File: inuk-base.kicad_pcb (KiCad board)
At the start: 2 copper layers, 159.8 x 99.8 mm, 11 parts, among them J1 Conn_02x05_Odd_Even, J2 Conn_01x06, J3 Conn_01x02_Male, J4 Conn_01x02_Male, U1 E73-2G4M04S-52832

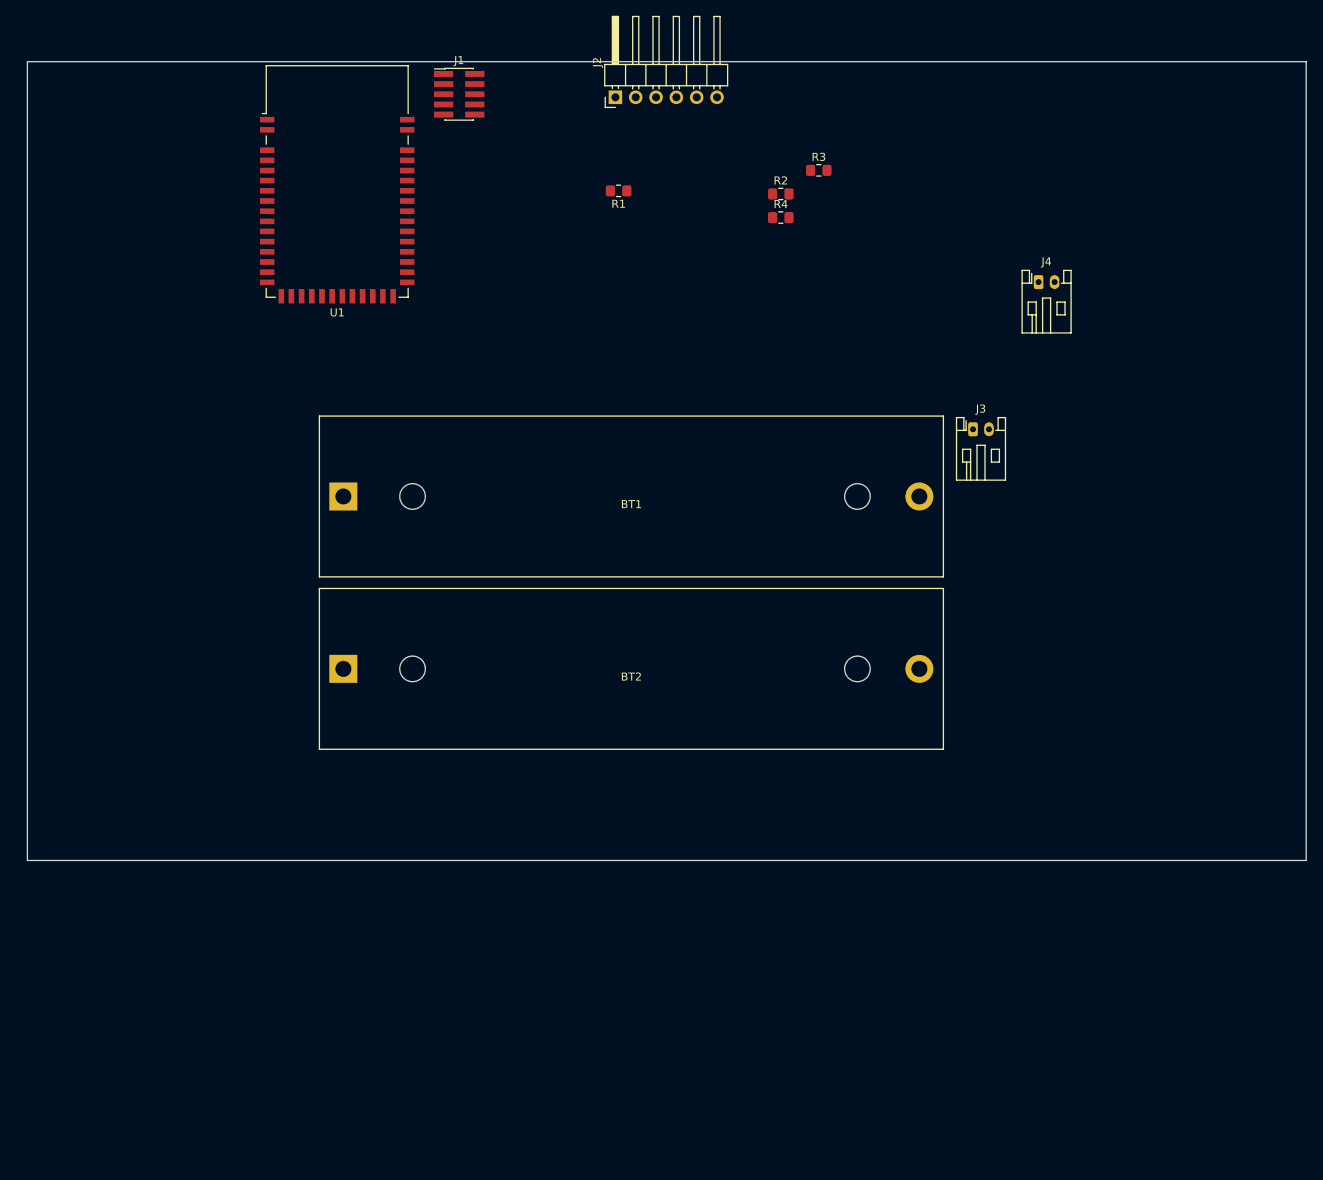
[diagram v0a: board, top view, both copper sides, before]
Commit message: added TP4056 module
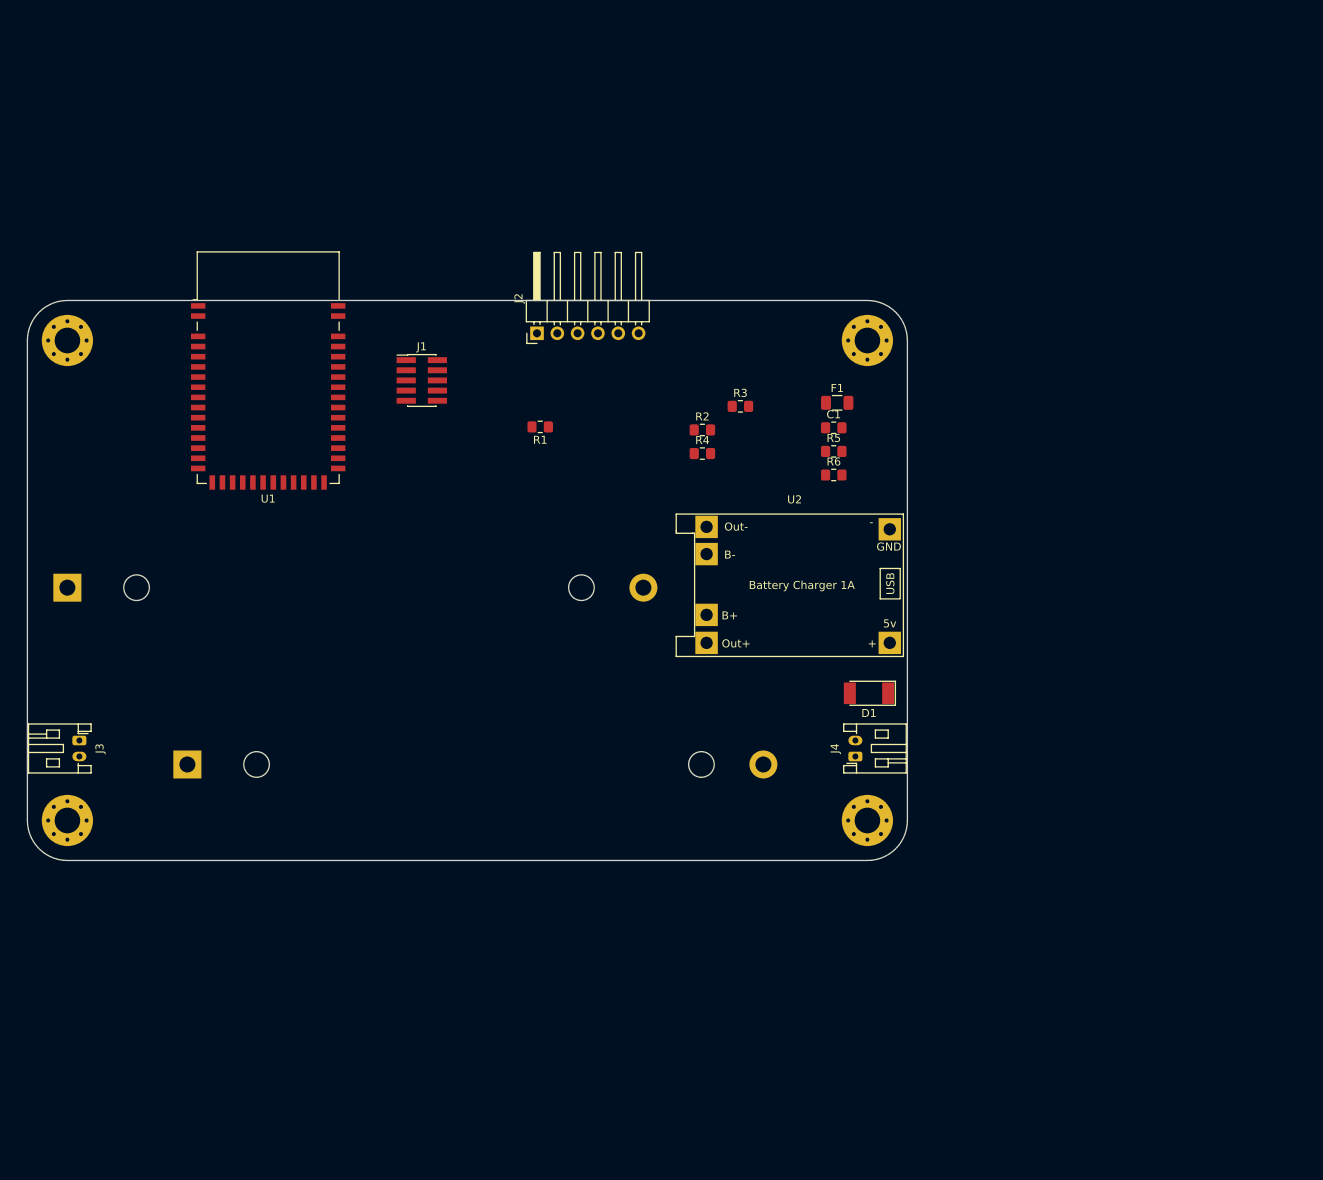
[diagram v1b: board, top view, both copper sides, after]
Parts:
- added C1: 1nF, Capacitor_SMD:C_0805_2012Metric_Pad1.15x1.40mm_HandSolder, F.Cu at (155.8, 90.9)
- added D1: SM4007, Diode_SMD:D_MELF, F.Cu at (160.2, 124.1)
- added F1: Fuse, Fuse:Fuse_1206_3216Metric, F.Cu at (156.2, 87.8)
- added H1: MountingHole, MountingHole:MountingHole_3.2mm_M3_Pad_Via, F.Cu at (60.0, 140.0)
- added H2: MountingHole, MountingHole:MountingHole_3.2mm_M3_Pad_Via, F.Cu at (60.0, 80.0)
- added H3: MountingHole, MountingHole:MountingHole_3.2mm_M3_Pad_Via, F.Cu at (160.0, 80.0)
- added H4: MountingHole, MountingHole:MountingHole_3.2mm_M3_Pad_Via, F.Cu at (160.0, 140.0)
- added R5: 806k, Resistor_SMD:R_0805_2012Metric_Pad1.15x1.40mm_HandSolder, F.Cu at (155.8, 93.9)
- added R6: 2M, Resistor_SMD:R_0805_2012Metric_Pad1.15x1.40mm_HandSolder, F.Cu at (155.8, 96.8)
- added U2: TP4056-module, Module:TP4056-module, F.Cu at (164.5, 119.5)
- BT1, BT2: moved to B.Cu
- moved J3 118.3 mm to (61.5, 130.0), turned to 270 degrees
- moved J4 63.6 mm to (158.5, 132.0), turned to 90 degrees
- moved BT1 36.3 mm to (60.0, 110.9)
- moved J1 36.1 mm to (104.3, 85.0)
- moved R1 31.1 mm to (119.1, 90.8)
- moved R2 31.1 mm to (139.4, 91.2)
- moved R3 31.1 mm to (144.1, 88.2)
- moved R4 31.1 mm to (139.4, 94.1)
- moved J2 31.1 mm to (118.7, 79.1)
- moved U1 24.8 mm to (85.1, 83.4)
- moved BT2 22.9 mm to (75.0, 133.0)
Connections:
- BT1 pad 2: Net-(BT1-Pad2) -> GND
- BT2 pad 1: Net-(BT2-Pad1) -> Net-(BT1-Pad1)
- BT2 pad 2: Net-(BT2-Pad2) -> GND
- J3 pad 1: Net-(J3-Pad1) -> +BATT
- J3 pad 2: Net-(J3-Pad2) -> GND
- J4 pad 2: Net-(J4-Pad2) -> GND
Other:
- board size 159.8 x 99.8 mm -> 110 x 70 mm

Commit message: pcb layout
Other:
- board text added: "Ext. battery"
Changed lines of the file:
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@@
   (general
     (thickness 1.6)
-    (drawings 8)
+    (drawings 9)
     (tracks 0)
     (zones 0)
@@
     )
   )
+  (gr_text "Ext. battery" (at 62.8 125.3) (layer F.SilkS)
+    (effects (font (size 1.5 1.5) (thickness 0.2)))
+  )
   (gr_arc (start 60 80) (end 55 80) (angle 90) (layer Edge.Cuts) (width 0.15))

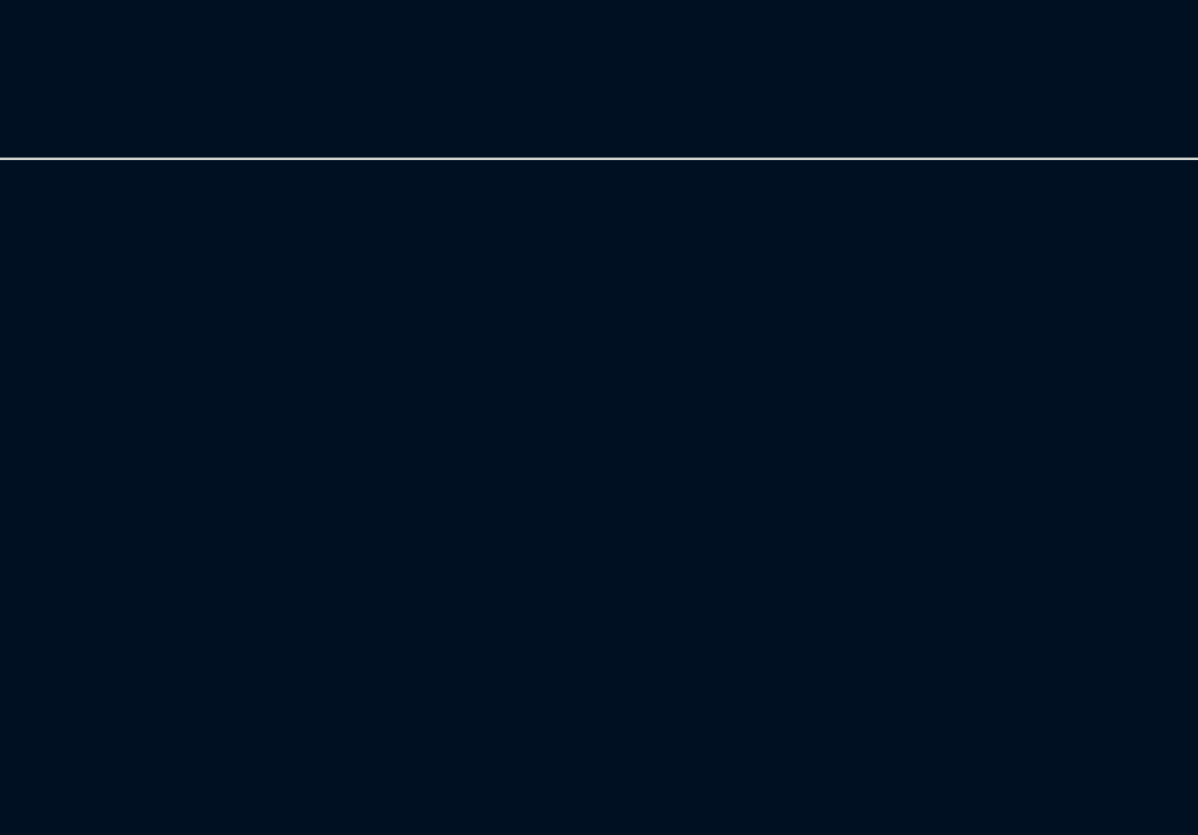
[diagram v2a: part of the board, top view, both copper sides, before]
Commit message: created light control schematic
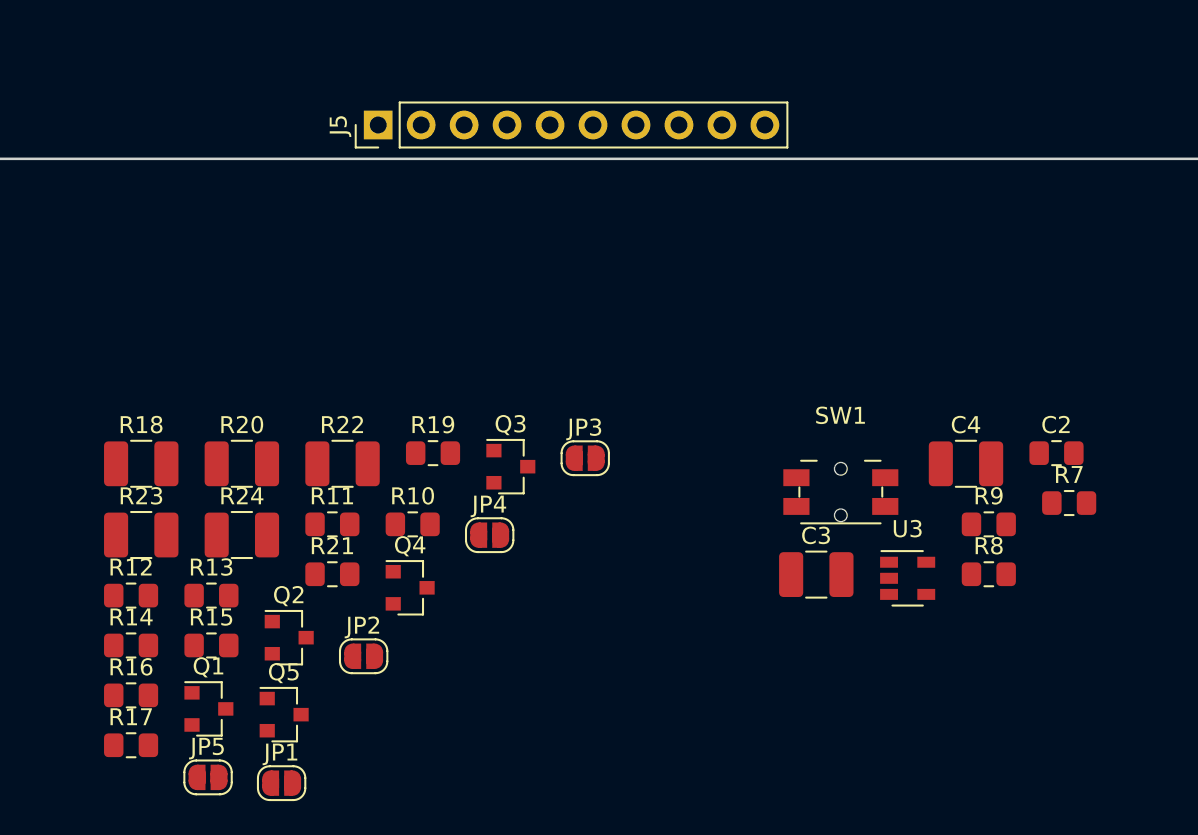
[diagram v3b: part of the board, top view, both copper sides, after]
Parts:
- added C2: 1nF, Capacitor_SMD:C_0805_2012Metric_Pad1.15x1.40mm_HandSolder, F.Cu at (140.1, 162.4)
- added C3: 10uF, Capacitor_SMD:C_1210_3225Metric_Pad1.42x2.65mm_HandSolder, F.Cu at (125.9, 169.6)
- added C4: 10uF, Capacitor_SMD:C_1210_3225Metric_Pad1.42x2.65mm_HandSolder, F.Cu at (134.8, 163.0)
- added J5: Conn_01x08, Connector_PinHeader_2.54mm:PinHeader_1x10_P2.54mm_Vertical, F.Cu at (100.0, 143.0)
- added JP1: Jumper_NO_Small, Jumper:SolderJumper-2_P1.3mm_Open_RoundedPad1.0x1.5mm, F.Cu at (94.3, 181.9)
- added JP2: Jumper_NO_Small, Jumper:SolderJumper-2_P1.3mm_Open_RoundedPad1.0x1.5mm, F.Cu at (99.1, 174.4)
- added JP3: Jumper_NO_Small, Jumper:SolderJumper-2_P1.3mm_Open_RoundedPad1.0x1.5mm, F.Cu at (112.2, 162.7)
- added JP4: Jumper_NO_Small, Jumper:SolderJumper-2_P1.3mm_Open_RoundedPad1.0x1.5mm, F.Cu at (106.6, 167.2)
- added JP5: Jumper_NO_Small, Jumper:SolderJumper-2_P1.3mm_Open_RoundedPad1.0x1.5mm, F.Cu at (89.9, 181.6)
- added Q1: DMG3406L, Package_TO_SOT_SMD:SOT-23, F.Cu at (90.0, 177.5)
- added Q2: DMG3406L, Package_TO_SOT_SMD:SOT-23, F.Cu at (94.7, 173.3)
- added Q3: DMG3406L, Package_TO_SOT_SMD:SOT-23, F.Cu at (107.8, 163.2)
- added Q4: DMG3406L, Package_TO_SOT_SMD:SOT-23, F.Cu at (101.9, 170.4)
- added Q5: DMG3406L, Package_TO_SOT_SMD:SOT-23, F.Cu at (94.4, 177.9)
- added R10: 100R, Resistor_SMD:R_0805_2012Metric_Pad1.15x1.40mm_HandSolder, F.Cu at (102.0, 166.6)
- added R11: 100R, Resistor_SMD:R_0805_2012Metric_Pad1.15x1.40mm_HandSolder, F.Cu at (97.3, 166.6)
- added R12: 100R, Resistor_SMD:R_0805_2012Metric_Pad1.15x1.40mm_HandSolder, F.Cu at (85.4, 170.8)
- added R13: 100R, Resistor_SMD:R_0805_2012Metric_Pad1.15x1.40mm_HandSolder, F.Cu at (90.1, 170.8)
- added R14: 100R, Resistor_SMD:R_0805_2012Metric_Pad1.15x1.40mm_HandSolder, F.Cu at (85.4, 173.8)
- added R15: 100k, Resistor_SMD:R_0805_2012Metric_Pad1.15x1.40mm_HandSolder, F.Cu at (90.1, 173.8)
- added R16: 100k, Resistor_SMD:R_0805_2012Metric_Pad1.15x1.40mm_HandSolder, F.Cu at (85.4, 176.7)
- added R17: 100k, Resistor_SMD:R_0805_2012Metric_Pad1.15x1.40mm_HandSolder, F.Cu at (85.4, 179.7)
- added R18: 0R5, Resistor_SMD:R_1210_3225Metric_Pad1.42x2.65mm_HandSolder, F.Cu at (86.0, 163.0)
- added R19: 100k, Resistor_SMD:R_0805_2012Metric_Pad1.15x1.40mm_HandSolder, F.Cu at (103.2, 162.4)
- added R20: 0R5, Resistor_SMD:R_1210_3225Metric_Pad1.42x2.65mm_HandSolder, F.Cu at (91.9, 163.0)
- added R21: 100k, Resistor_SMD:R_0805_2012Metric_Pad1.15x1.40mm_HandSolder, F.Cu at (97.3, 169.6)
- added R22: 0R5, Resistor_SMD:R_1210_3225Metric_Pad1.42x2.65mm_HandSolder, F.Cu at (97.9, 163.0)
- added R23: 0R5, Resistor_SMD:R_1210_3225Metric_Pad1.42x2.65mm_HandSolder, F.Cu at (86.0, 167.2)
- added R24: 0R5, Resistor_SMD:R_1210_3225Metric_Pad1.42x2.65mm_HandSolder, F.Cu at (91.9, 167.2)
- added R7: 2M, Resistor_SMD:R_0805_2012Metric_Pad1.15x1.40mm_HandSolder, F.Cu at (140.8, 165.3)
- added R8: 2M, Resistor_SMD:R_0805_2012Metric_Pad1.15x1.40mm_HandSolder, F.Cu at (136.1, 169.6)
- added R9: 100k, Resistor_SMD:R_0805_2012Metric_Pad1.15x1.40mm_HandSolder, F.Cu at (136.1, 166.6)
- added SW1: SW_DPST_x2, Button_Switch_SMD:Panasonic_EVQPUL_EVQPUC, F.Cu at (127.3, 164.7)
- added U3: AP2112K-3.3, Package_TO_SOT_SMD:SOT-23-5, F.Cu at (131.3, 169.8)
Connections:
- net Net-(D1-Pad1) renamed /power/VSOLAR

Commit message: layout
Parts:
- removed SW1: SW_DPST_x2, Button_Switch_SMD:Panasonic_EVQPUL_EVQPUC
- added C5: 100nF, Capacitor_SMD:C_0805_2012Metric_Pad1.15x1.40mm_HandSolder, F.Cu at (96.4, 140.9)
- J3: moved to B.Cu
- moved F1 104.1 mm to (61.4, 130.8), turned to 180 degrees
- moved R8 75.8 mm to (161.6, 98.2), turned to 270 degrees
- moved JP5 71.0 mm to (124.1, 119.3), turned to 270 degrees
- moved R14 69.8 mm to (117.9, 112.0), turned to 90 degrees
- moved R17 69.1 mm to (111.2, 115.6), turned to 180 degrees
- moved JP1 69.0 mm to (148.7, 139.4)
- moved R7 68.2 mm to (158.2, 99.4)
- moved C2 67.9 mm to (158.2, 97.0), turned to 180 degrees
- moved R12 64.2 mm to (111.3, 112.1), turned to 90 degrees
- moved R13 63.7 mm to (114.5, 112.0), turned to 90 degrees
- moved Q5 63.1 mm to (117.0, 118.9), turned to 270 degrees
- moved R15 60.5 mm to (106.3, 115.5), turned to 180 degrees
- moved Q1 60.4 mm to (106.2, 119.3), turned to 270 degrees
- moved R16 59.4 mm to (108.7, 122.1), turned to 180 degrees
- moved R21 57.5 mm to (117.0, 115.5), turned to 180 degrees
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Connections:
- J5 pad 1: Net-(J5-Pad1) -> +3V3
- Q2 pad 1: /light_ctrl/lio_1_sig -> /light_ctrl/lio_2_sig
- Q3 pad 1: /light_ctrl/lio_1_sig -> /light_ctrl/lio_3_sig
- Q4 pad 1: /light_ctrl/lio_1_sig -> /light_ctrl/lio_4_sig
- Q5 pad 1: /light_ctrl/lio_1_sig -> /light_ctrl/lio_5_sig
- R16 pad 1: /light_ctrl/lio_1_sig -> /light_ctrl/lio_2_sig
- R17 pad 1: /light_ctrl/lio_1_sig -> /light_ctrl/lio_3_sig
- R19 pad 1: /light_ctrl/lio_1_sig -> /light_ctrl/lio_4_sig
- R21 pad 1: /light_ctrl/lio_1_sig -> /light_ctrl/lio_5_sig
